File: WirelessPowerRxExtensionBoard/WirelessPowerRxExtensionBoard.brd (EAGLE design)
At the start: 100 x 80 mm, 33 parts, among them Q1 MOSFET-N, Q2 MOSFET-N, Q3 MOSFET-N

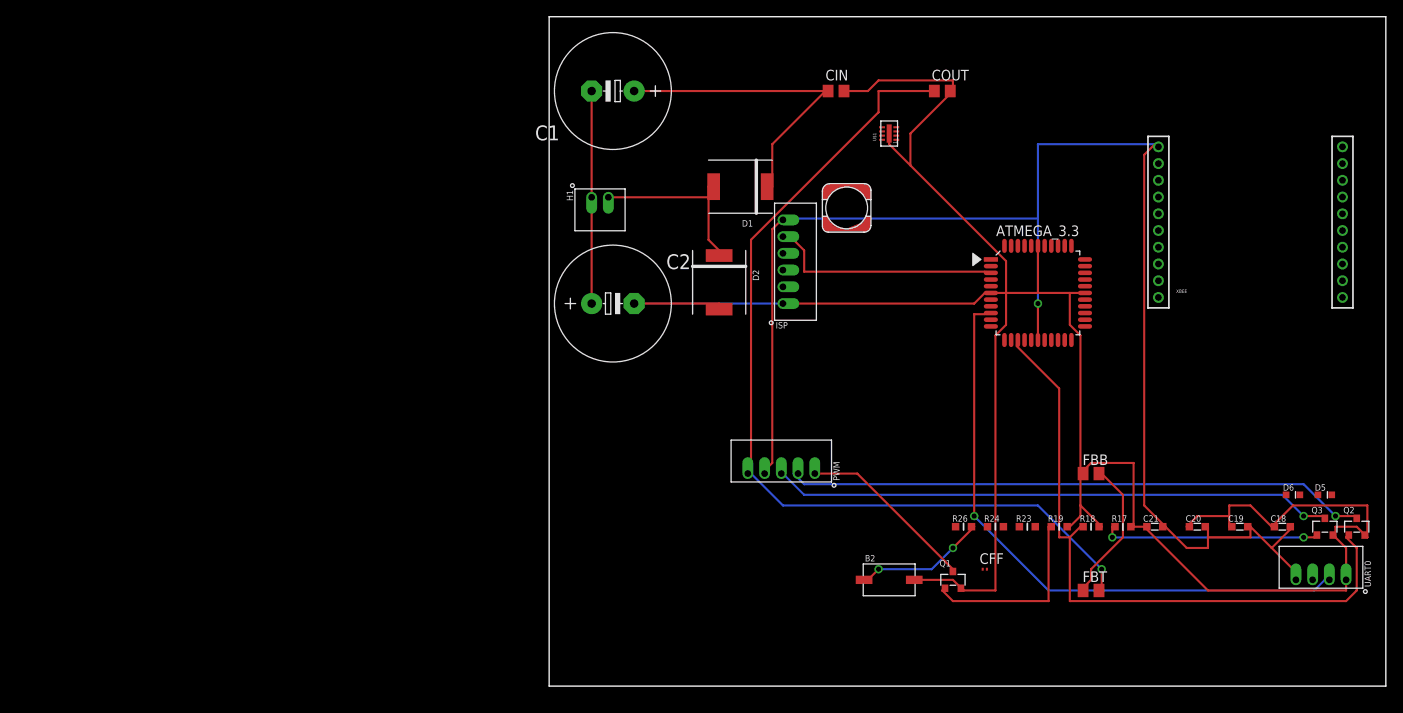
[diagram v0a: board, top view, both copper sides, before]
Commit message: Finished Schematic for Wireless Power Rx Extension Board
Also updated crawford library to include zener diode
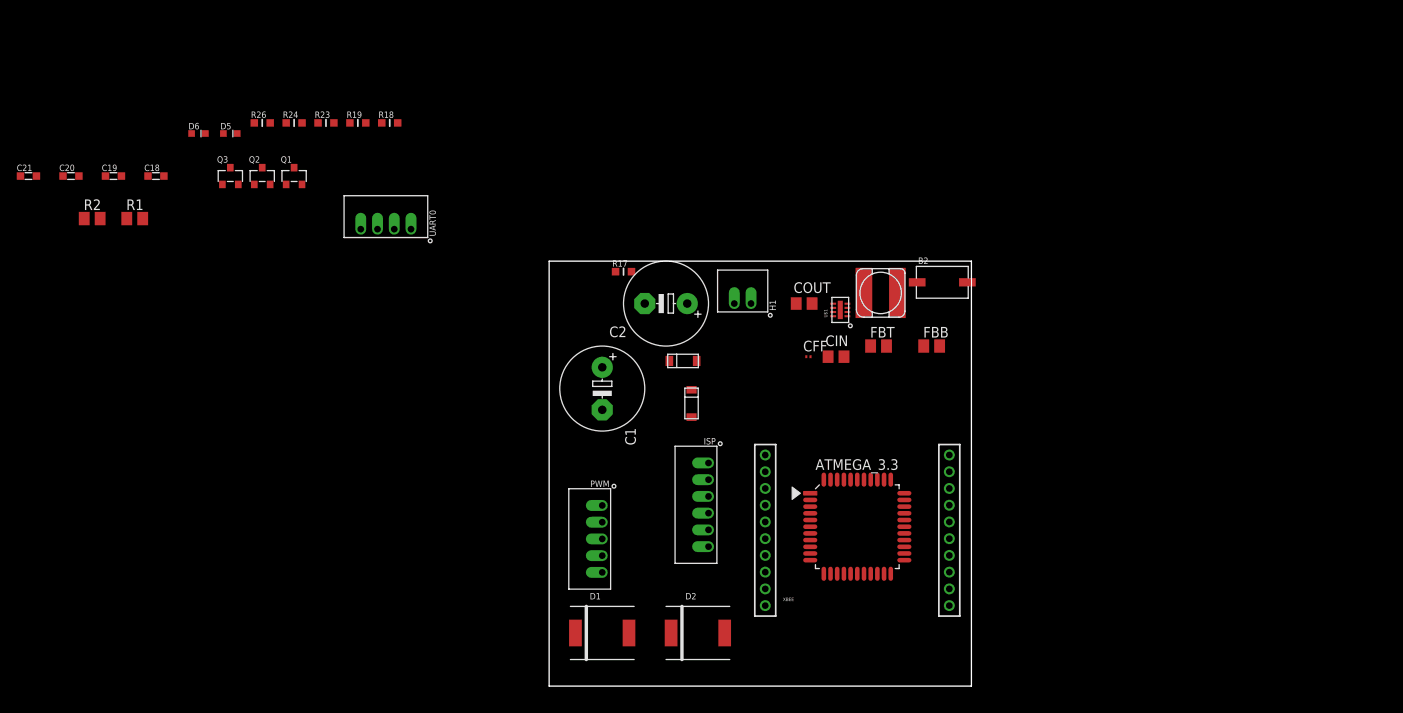
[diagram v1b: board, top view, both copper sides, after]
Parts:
- added R1, R2: 47K, resistor:M0805
- added Z1, Z2: ZENERDIODE, crawford:SOD-123
- C1, C2: value 9F -> 1.5F; device resistor:E5-13 -> resistor:E5-10,5
- moved C18 141.0 mm to (-47.0, 61.0)
- moved C19 141.0 mm to (-52.1, 61.0)
- moved C20 141.0 mm to (-57.1, 61.0)
- moved C21 141.0 mm to (-62.2, 61.0)
- moved D5 137.8 mm to (-38.1, 66.0)
- moved D6 137.8 mm to (-41.9, 66.0)
- moved Q2 137.4 mm to (-34.3, 61.0)
- moved Q3 137.4 mm to (-38.1, 61.0)
- moved UART0 119.4 mm to (-16.5, 54.6)
- moved R24 96.7 mm to (-30.5, 67.3)
- moved R18 96.7 mm to (-19.1, 67.3)
- moved R19 96.7 mm to (-22.9, 67.3)
- moved R23 96.7 mm to (-26.7, 67.3)
- moved R26 96.7 mm to (-34.3, 67.3)
- moved Q1 92.4 mm to (-30.5, 61.0)
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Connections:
- removed net N$2: C1.-, C2.+, H1.P$1
- removed net VRECT: CFF.1, COUT.1, FBT.2, PWM.P$5, U$1.4
- new net N$3: ATMEGA_3.3.37, R1.1, R2.2
- new net N$4: C1.-, C2.+, H1.P$1, Z1.P$2, Z2.P$1
- net 3.3V: now also CFF.1, COUT.1, FBT.2, U$1.4
- net GND: now also R2.1, Z2.P$2
- net VDOUBLE: now also PWM.P$5, R1.2, Z1.P$1
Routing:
- net GND: track 290.6 -> 0.00 mm
- net 3.3V: track 177.1 -> 0.00 mm, vias 1 -> 0
- net VRECT: track 109.0 -> 0.00 mm, vias 1 -> 0
- net PWM2: track 78.8 -> 0.00 mm
- net AT3_RX0: track 72.8 -> 0.00 mm, vias 1 -> 0
- net N$22: track 70.2 -> 0.00 mm, vias 1 -> 0
- net N$20: track 67.3 -> 0.00 mm, vias 1 -> 0
- net VDOUBLE: track 37.8 -> 0.00 mm
- net AT3_PR_SCK: track 28.3 -> 0.00 mm
- net PWM3: track 26.1 -> 0.00 mm, vias 2 -> 0
- net N$2: track 25.4 -> 0.00 mm
- net PWM1: track 22.9 -> 0.00 mm
- net N$1: track 22.7 -> 0.00 mm
- net N$24: track 21.5 -> 0.00 mm
- net FB: track 17.8 -> 0.00 mm
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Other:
- board size 100 x 80 mm -> 50.5 x 50.8 mm

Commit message: Lots of Routing progress
Routing!
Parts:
- moved R26 84.9 mm to (18.5, 0.86), turned to 180 degrees
- moved R2 78.5 mm to (5.99, 5.99), turned to 180 degrees
- moved R1 73.1 mm to (8.64, 11.5)
- moved C21 70.0 mm to (2.46, 34.1)
- moved C20 64.9 mm to (2.46, 35.4)
- moved R19 61.5 mm to (5.26, 12.6), turned to 270 degrees
- moved C19 59.8 mm to (2.57, 36.6)
- moved B2 58.4 mm to (11.2, 2.21), turned to 180 degrees
- moved Q3 58.1 mm to (2.31, 19.2)
- moved UART0 56.9 mm to (19.9, 10.8), turned to 90 degrees
- moved C18 54.8 mm to (2.69, 37.7)
- moved Q2 53.2 mm to (2.62, 22.7), turned to 270 degrees
- moved D6 52.1 mm to (2.54, 38.8)
- moved D5 48.4 mm to (2.62, 39.9)
- moved Q1 47.9 mm to (2.31, 26.1), turned to 270 degrees
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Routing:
- net 3.3V: track 0.00 -> 76.3 mm, vias 0 -> 2
- net GND: track 0.00 -> 47.6 mm
- net VDOUBLE: track 0.00 -> 35.8 mm
- net AT3_PR_SCK: track 0.00 -> 28.8 mm
- net AT3_BUTTON: track 0.00 -> 27.8 mm
- net AT3_PR_MISO: track 0.00 -> 27.4 mm
- net AT3_PR_MOSI: track 0.00 -> 25.2 mm
- net PWM3: track 0.00 -> 22.9 mm
- net PWM2: track 0.00 -> 21.7 mm
- net AT3_!RESET!: track 0.00 -> 21.6 mm, vias 0 -> 2
- net PWM1: track 0.00 -> 20.8 mm
- net N$1: track 0.00 -> 20.2 mm, vias 0 -> 2
- net AT3_TX1: track 0.00 -> 18.9 mm
- net AT3_LED2: track 0.00 -> 16.3 mm
- net AT3_TX0: track 0.00 -> 16.2 mm
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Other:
- board size 50.5 x 50.8 mm -> 50.9 x 51 mm

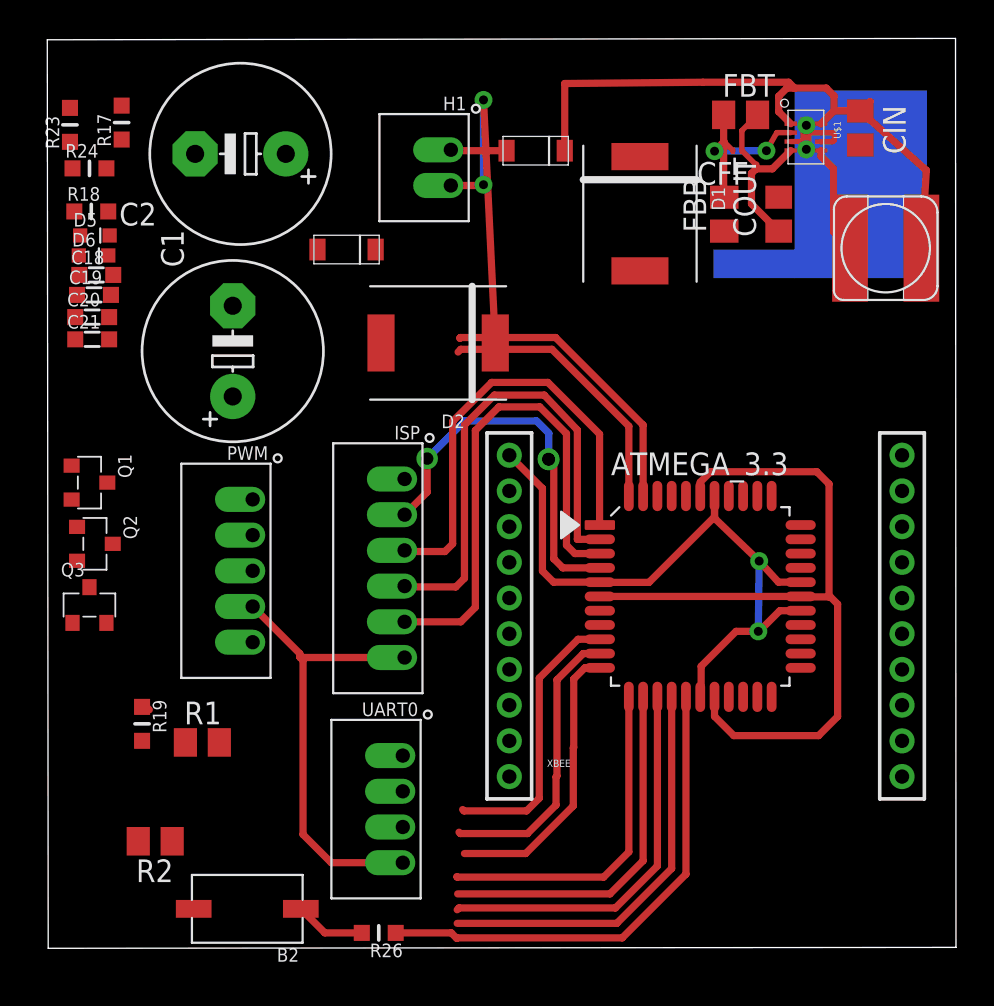
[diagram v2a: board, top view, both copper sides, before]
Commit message: Finished First Pass at Routing
still need to add vias to ground for voltage regulator
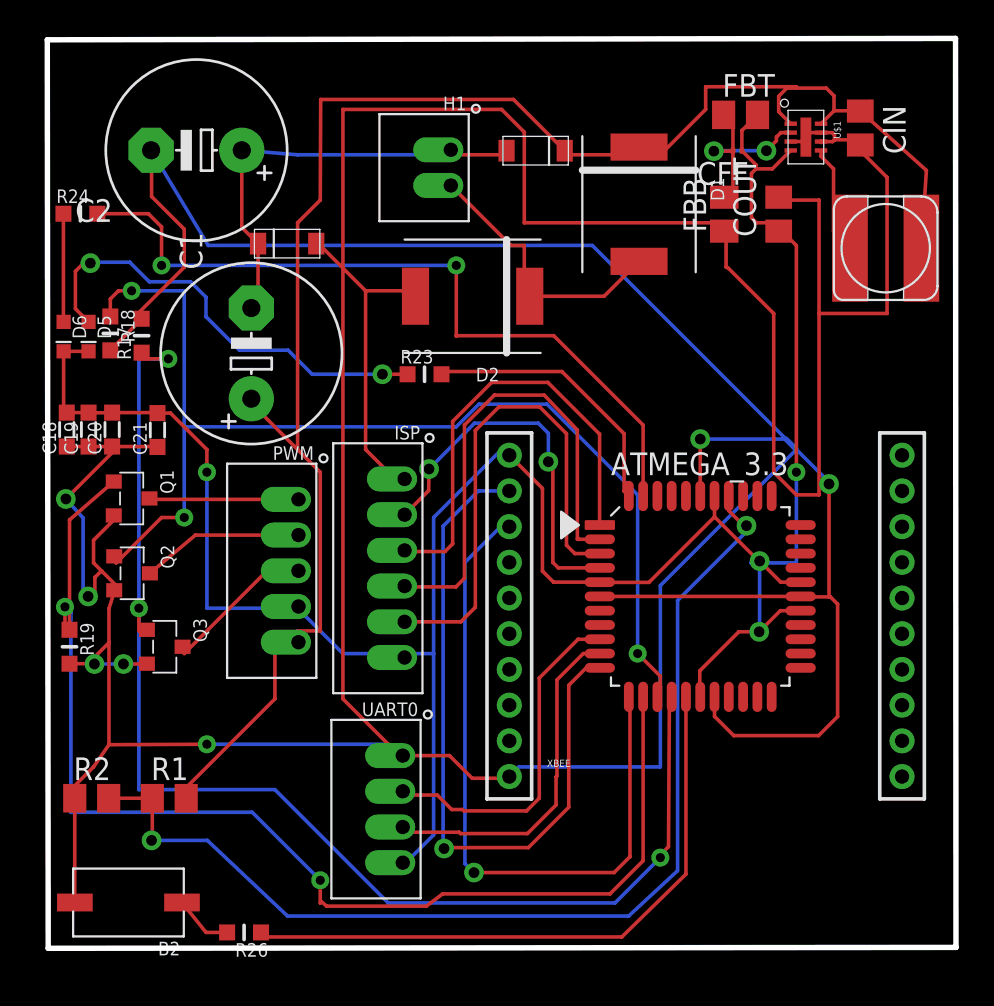
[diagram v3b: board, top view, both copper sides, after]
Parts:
- moved R23 24.3 mm to (21.1, 32.2), turned to 0 degrees
- moved R17 12.0 mm to (5.23, 34.3)
- moved C18 8.82 mm to (1.04, 29.1), turned to 90 degrees
- moved C19 7.55 mm to (2.26, 29.1), turned to 90 degrees
- moved R26 7.54 mm to (11.0, 0.89)
- moved R18 6.92 mm to (3.48, 34.4), turned to 270 degrees
- moved B2 6.66 mm to (4.50, 2.57)
- moved C20 6.40 mm to (3.58, 29.1), turned to 90 degrees
- moved C21 6.26 mm to (6.12, 29.0), turned to 90 degrees
- moved R19 5.93 mm to (1.19, 16.9)
- moved D5 5.68 mm to (2.26, 34.3), turned to 270 degrees
- moved D6 4.85 mm to (0.86, 34.3), turned to 270 degrees
- moved Q3 4.82 mm to (6.53, 16.9), turned to 270 degrees
- moved R2 4.30 mm to (2.44, 8.41), turned to 0 degrees
- moved R1 3.63 mm to (6.78, 8.41)
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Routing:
- net GND: track 47.6 -> 344.0 mm, vias 0 -> 7
- net VDOUBLE: track 35.8 -> 98.4 mm
- net N$3: track 0.00 -> 60.3 mm, vias 0 -> 2
- net 3.3V: track 76.3 -> 134.6 mm, vias 2 -> 4
- net PWM3: track 22.9 -> 71.7 mm, vias 0 -> 3
- net PWM1: track 20.8 -> 67.9 mm, vias 0 -> 2
- net PWM2: track 21.7 -> 63.8 mm, vias 0 -> 3
- net AT3_LED2: track 16.3 -> 43.0 mm, vias 0 -> 2
- net N$38: track 0.00 -> 25.2 mm, vias 0 -> 2
- net AT3_RX1: track 16.0 -> 39.5 mm, vias 0 -> 1
- net N$4: track 3.14 -> 24.4 mm
- net AT3_TX1: track 18.9 -> 39.0 mm, vias 0 -> 1
- net N$20: track 0.00 -> 9.29 mm
- net N$22: track 0.00 -> 9.10 mm
- net N$24: track 0.00 -> 8.37 mm
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
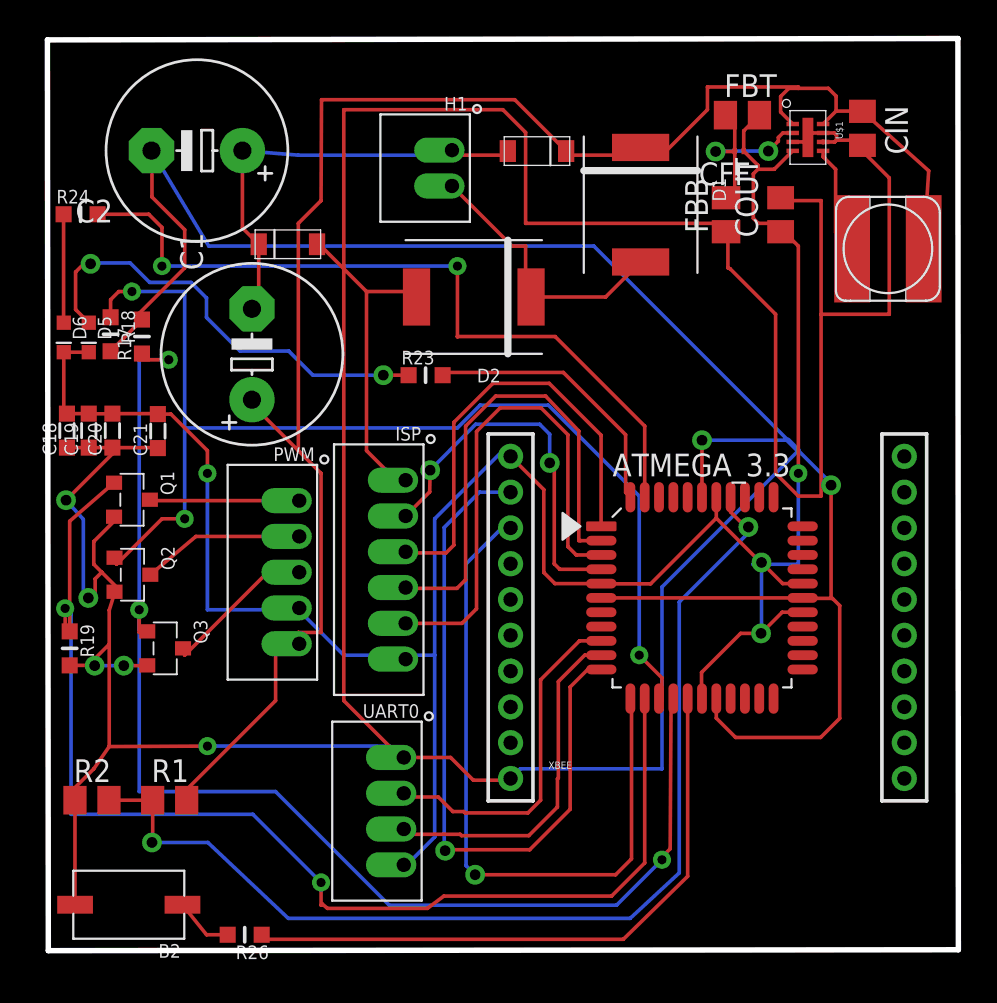
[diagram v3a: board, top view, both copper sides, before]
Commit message: Updated Routing
Re-routed power section with much larger traces and added ground plane.
Moved MCU resistors and caps under the radio but they still need to be
re-routed.
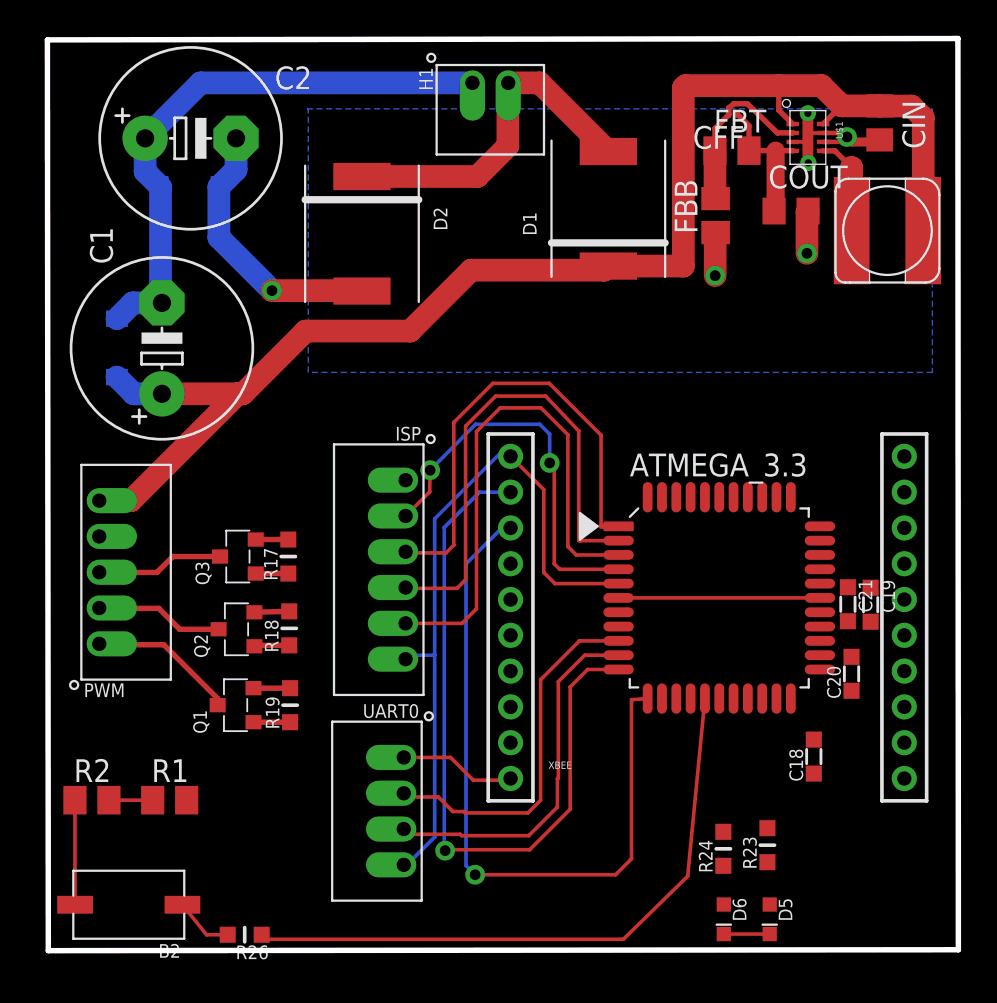
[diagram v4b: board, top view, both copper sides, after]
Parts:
- moved R24 50.5 mm to (37.7, 5.69), turned to 90 degrees
- moved D5 50.0 mm to (40.3, 1.75)
- moved D6 49.2 mm to (37.7, 1.75)
- moved C18 45.5 mm to (42.8, 10.8)
- moved C19 44.8 mm to (45.9, 19.3), turned to 270 degrees
- moved C20 43.5 mm to (44.9, 15.5)
- moved C21 39.8 mm to (44.7, 19.4), turned to 270 degrees
- moved R23 32.5 mm to (40.2, 5.89), turned to 90 degrees
- moved Z1 25.9 mm to (3.84, 33.7), flipped to the bottom, turned to 90 degrees
- moved R18 19.2 mm to (13.5, 18.0), turned to 90 degrees
- moved R17 14.8 mm to (13.4, 22.0)
- moved PWM 13.7 mm to (2.84, 17.1), turned to 270 degrees
- moved Q1 12.9 mm to (10.5, 13.7), turned to 90 degrees
- moved R19 12.7 mm to (13.5, 13.7), turned to 90 degrees
- moved D2 7.18 mm to (17.5, 40.1), turned to 270 degrees
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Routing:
- net GND: track 344.0 -> 56.3 mm, vias 7 -> 6
- net 3.3V: track 134.6 -> 50.1 mm, vias 4 -> 0
- net PWM3: track 71.7 -> 1.82 mm, vias 3 -> 0
- net PWM1: track 67.9 -> 2.05 mm, vias 2 -> 0
- net PWM2: track 63.8 -> 1.97 mm, vias 3 -> 0
- net N$3: track 60.3 -> 2.44 mm, vias 2 -> 0
- net AT3_LED2: track 43.0 -> 0.00 mm, vias 2 -> 0
- net N$38: track 25.2 -> 0.00 mm, vias 2 -> 0
- net VDOUBLE: track 98.4 -> 79.6 mm
- net AT3_LED1: track 15.3 -> 0.00 mm
- net N$4: track 24.4 -> 32.0 mm
- net N$39: track 6.06 -> 0.00 mm
- net N$1: track 15.4 -> 19.6 mm
- net N$20: track 9.29 -> 7.12 mm
- net N$22: track 9.10 -> 7.16 mm
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- added copper zone on layer 16, net GND

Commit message: First Routing Revision Complete
Much improved since the first routing!
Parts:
- R1: value 47K -> 47k; device resistor:M0805 -> carrick:R0603
- R2: device resistor:M0805 -> carrick:R0603
- moved R2 42.7 mm to (38.2, 31.6), turned to 90 degrees
- moved R1 39.0 mm to (36.6, 33.6), turned to 90 degrees
- moved C18 15.5 mm to (29.9, 19.6)
- moved C19 12.6 mm to (37.5, 28.7), turned to 0 degrees
- moved C20 7.68 mm to (38.4, 11.4), turned to 180 degrees
- moved H1 1.98 mm to (21.7, 48.5)
- moved C21 0.46 mm to (44.9, 19.0)
- moved D5 0.13 mm to (40.2, 1.75)
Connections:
- net GND: now also R2.P$1; no longer R2.1
- net N$3: now also R1.P$1, R2.P$2; no longer R1.1, R2.2
- net VDOUBLE: now also R1.P$2; no longer R1.2
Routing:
- net GND: track 56.3 -> 144.3 mm, vias 6 -> 12
- net 3.3V: track 50.1 -> 137.0 mm
- net PWM3: track 1.82 -> 56.8 mm, vias 0 -> 2
- net PWM2: track 1.97 -> 45.5 mm, vias 0 -> 2
- net AT3_LED1: track 0.00 -> 40.4 mm, vias 0 -> 2
- net PWM1: track 2.05 -> 38.5 mm
- net AT3_LED2: track 0.00 -> 35.7 mm, vias 0 -> 2
- net AT3_RX1: track 40.5 -> 15.3 mm
- net AT3_TX1: track 39.8 -> 18.1 mm
- net N$3: track 2.44 -> 18.0 mm, vias 0 -> 2
- net VDOUBLE: track 79.6 -> 88.5 mm
- net N$38: track 0.00 -> 2.37 mm
- net N$39: track 0.00 -> 2.17 mm
- net AT3_BUTTON: track 35.3 -> 37.4 mm
- net N$4: track 32.0 -> 30.1 mm
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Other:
- board text added: "CC"
- board text added: "V2.0"
